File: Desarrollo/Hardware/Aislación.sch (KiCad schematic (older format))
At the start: 26 parts, among them U11 ADuM6401, U12 ADuM2401, U13 NCP1117ST33T3G

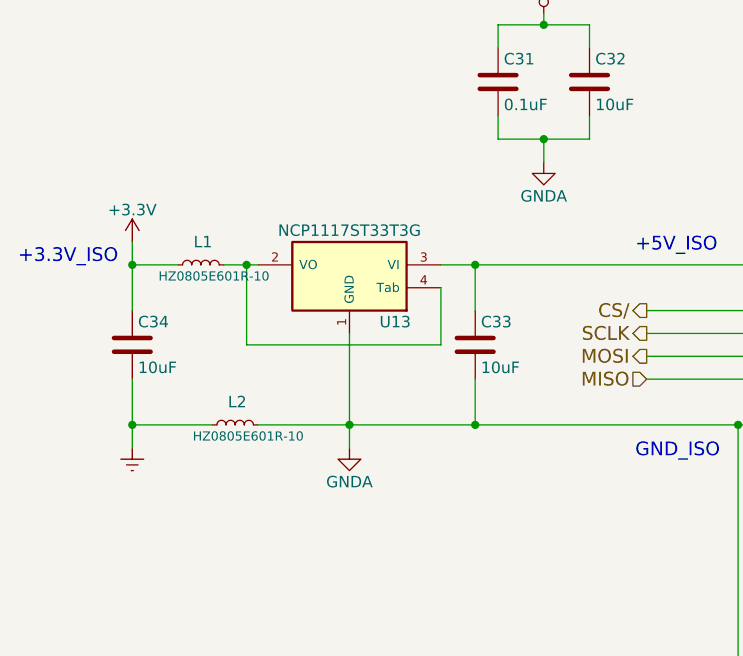
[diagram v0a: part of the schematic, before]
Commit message: Nueva actualización. Intercambio de tierras GNDA por DGND en hoja esquemático "Aislación". Ídem en hoja de "Protección". Además se hizo visible el nombre de la tierra digital DGND que no figuraba. Revisión FINAL. Cambios estéticos en ubicación de algunas pistas del PCB.
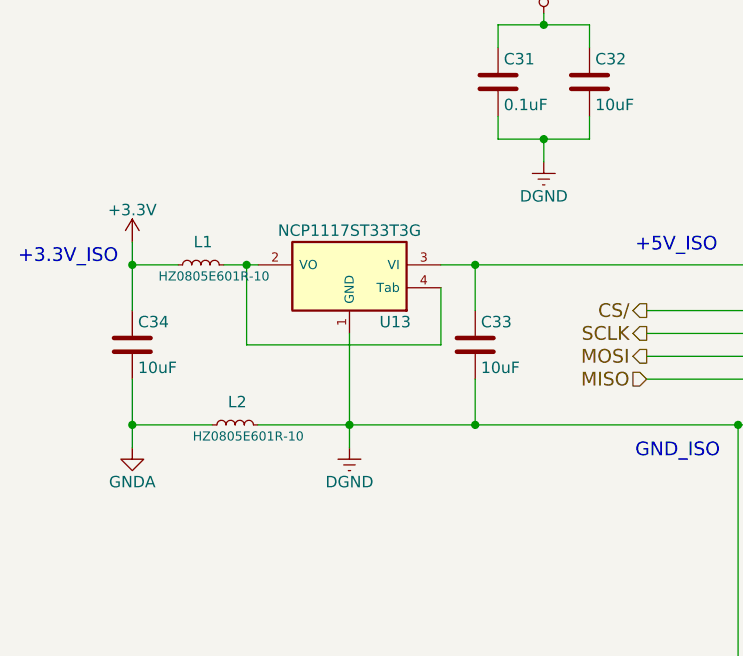
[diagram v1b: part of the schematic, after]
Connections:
- net DGND: now also C31.2, C32.2, C33.2, L2.2, U11.15 (GND_ISO), U11.9 (GND_ISO), U12.15 (GND2), U12.9 (GND2), U13.1 (GND); no longer C34.2, L2.1
- net GNDA: now also C34.2, L2.1; no longer C31.2, C32.2, C33.2, L2.2, U11.15 (GND_ISO), U11.9 (GND_ISO), U12.15 (GND2), U12.9 (GND2), U13.1 (GND)
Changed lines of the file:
@@
 L GNDA-RESCUE-PonchoERG #PWR032
 U 1 1 57CB14DA
+P 1050 2700
+F 0 "#PWR032" H 1050 2450 50  0001 C CNN
+F 1 "GNDA" H 1050 2550 50  0000 C CNN
+F 2 "" H 1050 2700 50  0000 C CNN
+F 3 "" H 1050 2700 50  0000 C CNN
+	1    1050 2700
+	1    0    0    -1
+$EndComp
+$Comp
+L DGND #PWR034
+U 1 1 57CB1526
 P 2000 2700
-F 0 "#PWR032" H 2000 2450 50  0001 C CNN
-F 1 "GNDA" H 2000 2550 50  0000 C CNN
+F 0 "#PWR034" H 2000 2450 50  0001 C CNN
+F 1 "DGND" H 2000 2550 50  0000 C CNN
 F 2 "" H 2000 2700 50  0000 C CNN
 F 3 "" H 2000 2700 50  0000 C CNN
 	1    2000 2700
-	1    0    0    -1
-$EndComp
-$Comp
-L GNDA-RESCUE-PonchoERG #PWR033
-U 1 1 57CB1500
-P 2850 1450
-F 0 "#PWR033" H 2850 1200 50  0001 C CNN
-F 1 "GNDA" H 2850 1300 50  0000 C CNN
-F 2 "" H 2850 1450 50  0000 C CNN
-F 3 "" H 2850 1450 50  0000 C CNN
-	1    2850 1450
-	1    0    0    -1
-$EndComp
-$Comp
-L DGND #PWR034
-U 1 1 57CB1526
-P 1050 2700
-F 0 "#PWR034" H 1050 2450 50  0001 C CNN
-F 1 "DGND" H 1050 2550 50  0001 C CNN
-F 2 "" H 1050 2700 50  0000 C CNN
-F 3 "" H 1050 2700 50  0000 C CNN
-	1    1050 2700
 	1    0    0    -1
 $EndComp
@@
 Text Label 7800 6100 2    60   ~ 0
 GND_NISO
+$Comp
+L DGND #PWR?
+U 1 1 580E54E8
+P 2850 1450
+F 0 "#PWR?" H 2850 1200 50  0001 C CNN
+F 1 "DGND" H 2850 1300 50  0000 C CNN
+F 2 "" H 2850 1450 50  0000 C CNN
+F 3 "" H 2850 1450 50  0000 C CNN
+	1    2850 1450
+	1    0    0    -1
+$EndComp
 $EndSCHEMATC

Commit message: Actualización final. Serigrafía nueva de jumpers y logos que se habían borrado de PONCHO y OPEN HARDWARE. PLACA TERMINADA.
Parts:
- added Slot_1: Fiducial, Fiducials:Fiducial_1mm_Dia_2.54mm_Outer_CopperTop, symbol Fiducial
- added Slot_2: Slot_2, Fiducials:Fiducial_1mm_Dia_2.54mm_Outer_CopperTop, symbol Fiducial
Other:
- note added: "In PCB:\nThe total lead length between both ends\nof the capacitor and the input power supply\npin should not exceed 20 mm"
- note added: "In PCB:\nThe total lead length between the ends of\nthe low ESR capacitor and the input power\nsupply pin must not exceed 2 mm."
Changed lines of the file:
@@
 LIBS:xilinx
 LIBS:Zilog
+LIBS:Jumpers_Config
+LIBS:Jumpers_Default
 LIBS:PonchoERG-cache
 EELAYER 25 0
@@
 Connection ~ 3700 3900
 Wire Wire Line
-	5150 3900 5400 3900
+	5400 3900 5150 3900
 Wire Wire Line
 	5400 2600 5400 4500
@@
 $EndComp
 $Comp
-L DGND #PWR034
+L DGND #PWR033
 U 1 1 57CB1526
 P 2000 2700
-F 0 "#PWR034" H 2000 2450 50  0001 C CNN
+F 0 "#PWR033" H 2000 2450 50  0001 C CNN
 F 1 "DGND" H 2000 2550 50  0000 C CNN
 F 2 "" H 2000 2700 50  0000 C CNN
@@
 P 1050 1800
 AR Path="/57CB154C" Ref="#PWR?"  Part="1"
-AR Path="/57BDC3A8/57CB154C" Ref="#PWR035"  Part="1"
-F 0 "#PWR035" H 1050 1650 50  0001 C CNN
+AR Path="/57BDC3A8/57CB154C" Ref="#PWR034"  Part="1"
+F 0 "#PWR034" H 1050 1650 50  0001 C CNN
 F 1 "+3.3V" H 1050 1940 50  0000 C CNN
 F 2 "" H 1050 1800 50  0000 C CNN
@@
 $EndComp
 $Comp
-L +5V #PWR036
+L +5V #PWR035
 U 1 1 57CB1572
 P 2850 800
-F 0 "#PWR036" H 2850 650 50  0001 C CNN
+F 0 "#PWR035" H 2850 650 50  0001 C CNN
 F 1 "+5V" H 2850 940 50  0000 C CNN
 F 2 "" H 2850 800 50  0000 C CNN
@@
 $EndComp
 $Comp
-L +5V #PWR037
+L +5V #PWR036
 U 1 1 57CB1598
 P 3800 1800
-F 0 "#PWR037" H 3800 1650 50  0001 C CNN
+F 0 "#PWR036" H 3800 1650 50  0001 C CNN
 F 1 "+5V" H 3800 1940 50  0000 C CNN
 F 2 "" H 3800 1800 50  0000 C CNN
@@
 Connection ~ 2550 1900
 Wire Wire Line
-	2550 2400 2550 2600
+	2550 2600 2550 2400
 Connection ~ 2550 2600
 Wire Wire Line
@@
 	1450 1900 1600 1900
 Wire Wire Line
-	1050 2700 1050 2400
+	1050 2400 1050 2700
 Wire Wire Line
 	1400 2600 1050 2600
@@
 $EndComp
 $Comp
-L GNDA #PWR038
+L GNDA #PWR037
 U 1 1 580D729E
 P 6800 6100
-F 0 "#PWR038" H 6800 6100 40  0001 C CNN
+F 0 "#PWR037" H 6800 6100 40  0001 C CNN
 F 1 "GNDA" H 6800 6030 40  0000 C CNN
 F 2 "" H 6800 6100 60  0000 C CNN
@@
 GND_NISO
 $Comp
-L DGND #PWR?
+L DGND #PWR038
 U 1 1 580E54E8
 P 2850 1450
-F 0 "#PWR?" H 2850 1200 50  0001 C CNN
+F 0 "#PWR038" H 2850 1200 50  0001 C CNN
 F 1 "DGND" H 2850 1300 50  0000 C CNN
 F 2 "" H 2850 1450 50  0000 C CNN
@@
 	1    0    0    -1
 $EndComp
+$Comp
+L Fiducial Slot_1
+U 1 1 5813B1F6
+P 4600 1400
+F 0 "Slot_1" H 4600 1600 60  0000 C CNN
+F 1 "Fiducial" H 4600 1200 60  0001 C CNN
+F 2 "Fiducials:Fiducial_1mm_Dia_2.54mm_Outer_CopperTop" H 4600 1400 60  0001 C CNN
+F 3 "" H 4600 1400 60  0000 C CNN
+	1    4600 1400
+	1    0    0    -1
+$EndComp
+$Comp
+L Fiducial Slot_2
+U 1 1 5813B95D
+P 4600 5050
+F 0 "Slot_2" H 4600 5250 60  0000 C CNN
+F 1 "Slot_2" H 4600 4850 60  0001 C CNN
+F 2 "Fiducials:Fiducial_1mm_Dia_2.54mm_Outer_CopperTop" H 4600 5050 60  0001 C CNN
+F 3 "" H 4600 5050 60  0000 C CNN
+	1    4600 5050
+	1    0    0    -1
+$EndComp
+Text Notes 5950 3650 0    60   ~ 12
+In PCB:\nThe total lead length between both ends\nof the capacitor and the input power supply\npin should not exceed 20 mm
+Wire Notes Line
+	5400 1850 6150 1850
+Wire Notes Line
+	5400 950  7500 950
+Wire Notes Line
+	7500 950  7500 1400
+Wire Notes Line
+	5400 950  5400 1850
+Wire Notes Line
+	7500 1400 6150 1400
+Wire Notes Line
+	6150 1400 6150 1850
+Text Notes 5450 1350 0    60   ~ 12
+In PCB:\nThe total lead length between the ends of\nthe low ESR capacitor and the input power\nsupply pin must not exceed 2 mm.
+Wire Notes Line
+	5500 3200 8100 3200
+Wire Notes Line
+	8100 3200 8100 3750
+Wire Notes Line
+	8100 3750 5500 3750
+Wire Notes Line
+	5500 3750 5500 3200
 $EndSCHEMATC

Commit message: Corrección de etiqueta de serigrafía en J2. Se cambió GPIO_3 que estaba repetido por GPIO_4.
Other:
- note added: "En PCB:\nZona de corte para seguridad ADuM2401"
- note added: "En PCB:\nZona de corte para seguridad ADuM6401"
- moved on the sheet: C31, C32
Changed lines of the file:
@@
 L C C31
 U 1 1 57C3B1DA
-P 2650 1100
-F 0 "C31" H 2675 1200 50  0000 L CNN
-F 1 "0.1uF" H 2675 1000 50  0000 L CNN
-F 2 "Capacitors_SMD:C_0805" H 2688 950 50  0001 C CNN
-F 3 "http://www.kemet.com/Lists/ProductCatalog/Attachments/53/KEM_C1002_X7R_SMD.pdf" H 2650 1100 50  0001 C CNN
-	1    2650 1100
+P 2250 1050
+F 0 "C31" H 2275 1150 50  0000 L CNN
+F 1 "0.1uF" H 2275 950 50  0000 L CNN
+F 2 "Capacitors_SMD:C_0805" H 2288 900 50  0001 C CNN
+F 3 "http://www.kemet.com/Lists/ProductCatalog/Attachments/53/KEM_C1002_X7R_SMD.pdf" H 2250 1050 50  0001 C CNN
+	1    2250 1050
 	1    0    0    -1
 $EndComp
@@
 L C C32
 U 1 1 57C3B223
-P 3050 1100
-F 0 "C32" H 3075 1200 50  0000 L CNN
-F 1 "10uF" H 3075 1000 50  0000 L CNN
-F 2 "Capacitors_SMD:C_0805" H 3088 950 50  0001 C CNN
-F 3 "http://www.kemet.com/Lists/ProductCatalog/Attachments/19/KEM_C1006_X5R_SMD.pdf" H 3050 1100 50  0001 C CNN
-	1    3050 1100
-	1    0    0    -1
-$EndComp
-Wire Wire Line
-	2650 950  2650 850
-Wire Wire Line
-	2650 850  3050 850
-Wire Wire Line
-	3050 850  3050 950
-Connection ~ 2850 850
-Wire Wire Line
-	2650 1250 2650 1350
-Wire Wire Line
-	2650 1350 3050 1350
-Wire Wire Line
-	3050 1350 3050 1250
-Connection ~ 2850 1350
+P 2650 1050
+F 0 "C32" H 2675 1150 50  0000 L CNN
+F 1 "10uF" H 2675 950 50  0000 L CNN
+F 2 "Capacitors_SMD:C_0805" H 2688 900 50  0001 C CNN
+F 3 "http://www.kemet.com/Lists/ProductCatalog/Attachments/19/KEM_C1006_X5R_SMD.pdf" H 2650 1050 50  0001 C CNN
+	1    2650 1050
+	1    0    0    -1
+$EndComp
+Wire Wire Line
+	2250 900  2250 800
+Wire Wire Line
+	2250 800  2650 800
+Wire Wire Line
+	2650 800  2650 900
+Connection ~ 2450 800
+Wire Wire Line
+	2250 1200 2250 1300
+Wire Wire Line
+	2250 1300 2650 1300
+Wire Wire Line
+	2650 1300 2650 1200
+Connection ~ 2450 1300
 Wire Wire Line
 	3800 1800 3800 4400
 Connection ~ 3800 2500
 Wire Wire Line
-	2850 800  2850 850
-Wire Wire Line
-	2850 1350 2850 1450
+	2450 750  2450 800
+Wire Wire Line
+	2450 1300 2450 1400
 $Comp
 L ADuM6401-RESCUE-PonchoERG U11
@@
 P 4600 4150
 F 0 "U12" H 4300 4650 60  0000 C CNN
-F 1 "ADuM2401" H 4500 3650 60  0000 C CNN
+F 1 "ADuM2401" H 4850 4650 60  0000 C CNN
 F 2 "SMD_Packages:SO-16-W" H 4600 4150 60  0001 C CNN
 F 3 "http://www.analog.com/media/en/technical-documentation/data-sheets/ADuM2400_2401_2402.pdf" H 4600 4150 60  0001 C CNN
@@
 L +5V #PWR035
 U 1 1 57CB1572
-P 2850 800
-F 0 "#PWR035" H 2850 650 50  0001 C CNN
-F 1 "+5V" H 2850 940 50  0000 C CNN
-F 2 "" H 2850 800 50  0000 C CNN
-F 3 "" H 2850 800 50  0000 C CNN
-	1    2850 800
+P 2450 750
+F 0 "#PWR035" H 2450 600 50  0001 C CNN
+F 1 "+5V" H 2450 890 50  0000 C CNN
+F 2 "" H 2450 750 50  0000 C CNN
+F 3 "" H 2450 750 50  0000 C CNN
+	1    2450 750
 	1    0    0    -1
 $EndComp
@@
 L DGND #PWR038
 U 1 1 580E54E8
-P 2850 1450
-F 0 "#PWR038" H 2850 1200 50  0001 C CNN
-F 1 "DGND" H 2850 1300 50  0000 C CNN
-F 2 "" H 2850 1450 50  0000 C CNN
-F 3 "" H 2850 1450 50  0000 C CNN
-	1    2850 1450
+P 2450 1400
+F 0 "#PWR038" H 2450 1150 50  0001 C CNN
+F 1 "DGND" H 2450 1250 50  0000 C CNN
+F 2 "" H 2450 1400 50  0000 C CNN
+F 3 "" H 2450 1400 50  0000 C CNN
+	1    2450 1400
 	1    0    0    -1
 $EndComp
@@
 Wire Notes Line
 	5500 3750 5500 3200
+Text Notes 4250 5100 2    60   ~ 0
+En PCB:\nZona de corte para seguridad ADuM2401
+Text Notes 3350 1100 0    60   ~ 0
+En PCB:\nZona de corte para seguridad ADuM6401
+Wire Notes Line
+	4350 1750 4350 1150
+Wire Notes Line
+	4350 1150 4850 1150
+Wire Notes Line
+	4850 1150 4850 1750
+Wire Notes Line
+	4350 4600 4350 5250
+Wire Notes Line
+	4350 5250 4850 5250
+Wire Notes Line
+	4850 5250 4850 4600
 $EndSCHEMATC
